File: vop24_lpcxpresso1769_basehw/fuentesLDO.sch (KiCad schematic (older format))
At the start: 21 parts, among them J101 Conn_01x03_Male, U101 MCP1700T-3302E_TT, U102 MCP1700T-3302E_TT, U103 TPS63001

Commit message: PCB: posicionamiento preruteo. ESQ: cambio de footprint de conectores
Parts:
- FB101: symbol dk_Ferrite-Beads-and-Chips:BLM21PG331SN1D -> vop24_lpcxpresso1769_basehw-rescue:BLM21PG331SN1D-dk_Ferrite-Beads-and-Chips
- J101: symbol Connector:Conn_01x03_Male -> vop24_lpcxpresso1769_basehw-rescue:Conn_01x03_Male-Connector
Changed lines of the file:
@@
 DVCC_UD
 $Comp
-L Connector:Conn_01x03_Male J101
+L vop24_lpcxpresso1769_basehw-rescue:Conn_01x03_Male-Connector J101
 U 1 1 5BC24F14
 P 9750 3200
+AR Path="/5BC24F14" Ref="J101"  Part="1"
+AR Path="/5B3826CA/5BC24F14" Ref="J101"  Part="1"
 F 0 "J101" H 9856 3478 50  0000 C CNN
 F 1 "Conn_01x03_Male" H 9856 3387 50  0000 C CNN
@@
 	8900 3200 9550 3200
 $Comp
-L dk_Ferrite-Beads-and-Chips:BLM21PG331SN1D FB101
+L vop24_lpcxpresso1769_basehw-rescue:BLM21PG331SN1D-dk_Ferrite-Beads-and-Chips FB101
 U 1 1 5BD41945
 P 5500 6400
+AR Path="/5BD41945" Ref="FB101"  Part="1"
+AR Path="/5B3826CA/5BD41945" Ref="FB101"  Part="1"
 F 0 "FB101" H 5500 6687 60  0000 C CNN
 F 1 "BLM21PG331SN1D" H 5500 6581 60  0000 C CNN

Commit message: PCB: ruteo de fuentes.    SCH: separacion de pistas de masa en fuentes
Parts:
- added R101: 0, Resistor_SMD:R_0805_2012Metric_Pad1.15x1.40mm_HandSolder, symbol Device:R_Small
- renumbered R101 to R102, R102 to R103, R103 to R104, R104 to R105, R105 to R106
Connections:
- wire segments 95 -> 96
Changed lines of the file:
@@
 $EndComp
 $Comp
-L Device:R_Small R101
+L Device:R_Small R102
 U 1 1 5B383133
 P 3250 4150
-F 0 "R101" V 3150 4050 50  0000 L CNN
+F 0 "R102" V 3150 4050 50  0000 L CNN
 F 1 "0" V 3200 4250 50  0000 L CNN
 F 2 "Resistor_SMD:R_0805_2012Metric_Pad1.15x1.40mm_HandSolder" H 3250 4150 50  0001 C CNN
@@
 $EndComp
 $Comp
-L Device:R_Small R102
+L Device:R_Small R103
 U 1 1 5B38313A
 P 3300 5350
-F 0 "R102" V 3200 5250 50  0000 L CNN
+F 0 "R103" V 3200 5250 50  0000 L CNN
 F 1 "0" V 3250 5500 50  0000 L CNN
 F 2 "Resistor_SMD:R_0805_2012Metric_Pad1.15x1.40mm_HandSolder" H 3300 5350 50  0001 C CNN
@@
 	0    1    1    0
 $EndComp
-Text Label 5000 3500 0    60   ~ 0
-DVCC
 Text Label 5000 4150 0    60   ~ 0
 DGND
@@
 $EndComp
 $Comp
-L Device:R_Small R104
+L Device:R_Small R105
 U 1 1 5B38314E
 P 5950 4000
-F 0 "R104" H 5980 4020 50  0000 L CNN
+F 0 "R105" H 5980 4020 50  0000 L CNN
 F 1 "1k" H 5980 3960 50  0000 L CNN
 F 2 "Resistor_SMD:R_0805_2012Metric_Pad1.15x1.40mm_HandSolder" H 5950 4000 50  0001 C CNN
@@
 $EndComp
 $Comp
-L Device:R_Small R105
+L Device:R_Small R106
 U 1 1 5B38315C
 P 5950 5200
-F 0 "R105" H 5980 5220 50  0000 L CNN
+F 0 "R106" H 5980 5220 50  0000 L CNN
 F 1 "1k" H 5980 5160 50  0000 L CNN
 F 2 "Resistor_SMD:R_0805_2012Metric_Pad1.15x1.40mm_HandSolder" H 5950 5200 50  0001 C CNN
@@
 $EndComp
 $Comp
-L Device:R R103
+L Device:R R104
 U 1 1 5BBFC68E
 P 4600 2300
-F 0 "R103" H 4670 2346 50  0000 L CNN
+F 0 "R104" H 4670 2346 50  0000 L CNN
 F 1 "100" H 4670 2255 50  0000 L CNN
 F 2 "Resistor_SMD:R_0805_2012Metric_Pad1.15x1.40mm_HandSolder" V 4530 2300 50  0001 C CNN
@@
 Wire Wire Line
 	2700 3600 2700 3000
-Wire Wire Line
-	2700 3000 3800 3000
 Connection ~ 2700 3600
 Wire Wire Line
 	2700 3600 2600 3600
-Connection ~ 3800 3000
 Text HLabel 7550 3000 2    60   BiDi ~ 0
 DGND
@@
 DVCC_UD
 $Comp
-L vop24_lpcxpresso1769_basehw-rescue:Conn_01x03_Male-Connector J101
+L vop24_lpcxpresso1769_basehw-rescue:Conn_01x03_Male-Connector J?
 U 1 1 5BC24F14
 P 9750 3200
-AR Path="/5BC24F14" Ref="J101"  Part="1"
+AR Path="/5BC24F14" Ref="J?"  Part="1"
 AR Path="/5B3826CA/5BC24F14" Ref="J101"  Part="1"
 F 0 "J101" H 9856 3478 50  0000 C CNN
@@
 	8900 3200 9550 3200
 $Comp
-L vop24_lpcxpresso1769_basehw-rescue:BLM21PG331SN1D-dk_Ferrite-Beads-and-Chips FB101
+L vop24_lpcxpresso1769_basehw-rescue:BLM21PG331SN1D-dk_Ferrite-Beads-and-Chips FB?
 U 1 1 5BD41945
 P 5500 6400
-AR Path="/5BD41945" Ref="FB101"  Part="1"
+AR Path="/5BD41945" Ref="FB?"  Part="1"
 AR Path="/5B3826CA/5BD41945" Ref="FB101"  Part="1"
 F 0 "FB101" H 5500 6687 60  0000 C CNN
@@
 Wire Wire Line
 	5700 6400 6250 6400
+$Comp
+L Device:R_Small R101
+U 1 1 5BEC88E2
+P 3250 3000
+F 0 "R101" V 3150 2900 50  0000 L CNN
+F 1 "0" V 3200 3100 50  0000 L CNN
+F 2 "Resistor_SMD:R_0805_2012Metric_Pad1.15x1.40mm_HandSolder" H 3250 3000 50  0001 C CNN
+F 3 "" H 3250 3000 50  0001 C CNN
+	1    3250 3000
+	0    1    1    0
+$EndComp
+Wire Wire Line
+	3350 3000 3800 3000
+Connection ~ 3800 3000
+Wire Wire Line
+	3150 3000 2700 3000
 $EndSCHEMATC

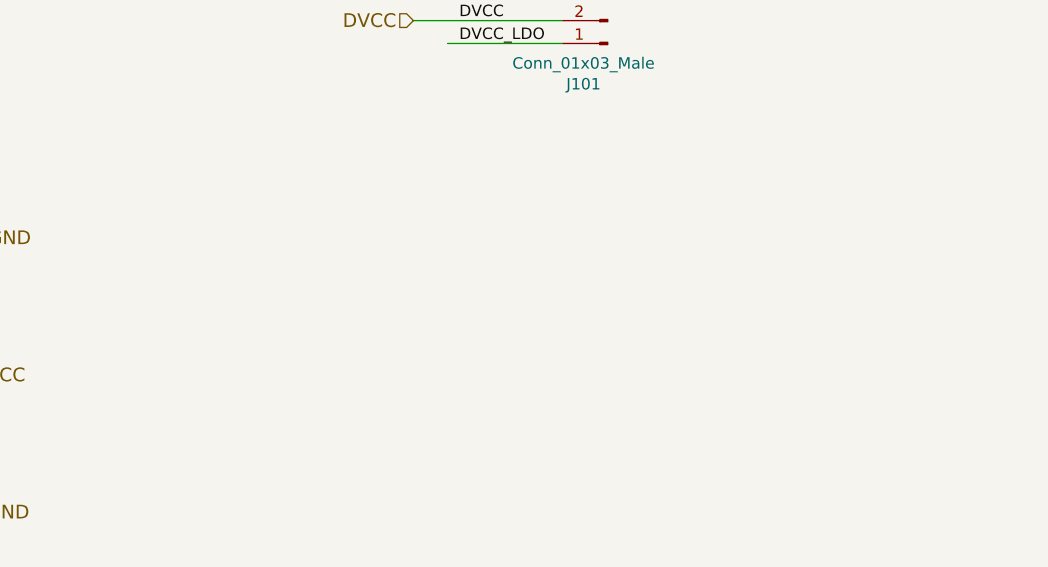
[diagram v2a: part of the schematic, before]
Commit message: Agregado de leyendas en PCB y ESQ. Agregado de cotas en PCB
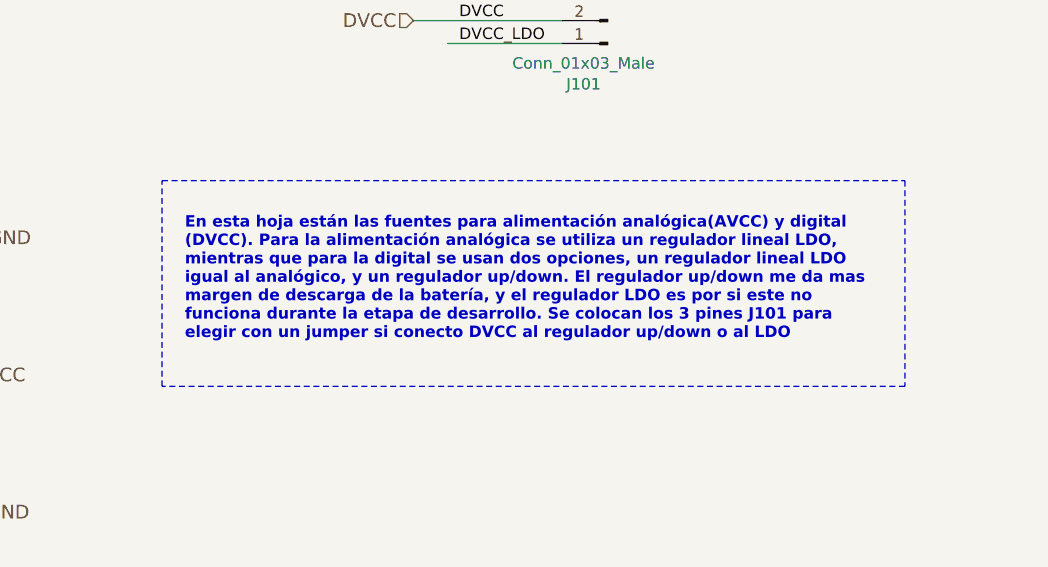
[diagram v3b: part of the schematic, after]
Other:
- note added: "En esta hoja están las fuentes para alimentación analógica(AVCC) y digital\n(DVCC). Para la alimentación analógica se utiliza un regulador lineal LDO,\nmientras que para la digital se usan dos opciones, un regulador lineal LDO\nigual al analógico, y un regulador up/down. El regulador up/down me da mas\nmargen de descarga de la batería, y el regulador LDO es por si este no\nfunciona durante la eta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"
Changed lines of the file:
@@
 encoding utf-8
 Sheet 4 5
-Title ""
-Date ""
-Rev ""
-Comp ""
-Comment1 ""
+Title "VOP24 - Reguladores Analógico y Digital"
+Date "2018-11-01"
+Rev "0.1"
+Comp "Federico G. Roux"
+Comment1 "Universidad Favaloro"
 Comment2 ""
 Comment3 ""
@@
 Wire Wire Line
 	3150 3000 2700 3000
+Text Notes 7900 4600 0    50   ~ 10
+En esta hoja están las fuentes para alimentación analógica(AVCC) y digital\n(DVCC). Para la alimentación analógica se utiliza un regulador lineal LDO,\nmientras que para la digital se usan dos opciones, un regulador lineal LDO\nigual al analógico, y un regulador up/down. El regulador up/down me da mas\nmargen de descarga de la batería, y el regulador LDO es por si este no\nfunciona durante la etapa de desarrollo. Se colocan los 3 pines J101 para\nelegir con un jumper si conecto DVCC al regulador up/down o al LDO\n
+Wire Notes Line
+	7800 3900 11050 3900
+Wire Notes Line
+	11050 3900 11050 4800
+Wire Notes Line
+	11050 4800 7800 4800
+Wire Notes Line
+	7800 4800 7800 3900
 $EndSCHEMATC

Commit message: ESQ: cambios sobre etiquetas y simbolos de POWER
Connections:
- net labels added: GNDA, GNDD, GNDREF, VCOM
- net labels removed: GNDBAT, GND_NREG, VBAT, VCC_NREG
- wire segments 96 -> 99
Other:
- note added: "Tensión no regulada que\nproviene de VUSB si está\nconectado, o de +BATT"
- moved on the sheet: C101, C102, C103, C104, C105, C106, C107, C108, D101, D102, FB101, J101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

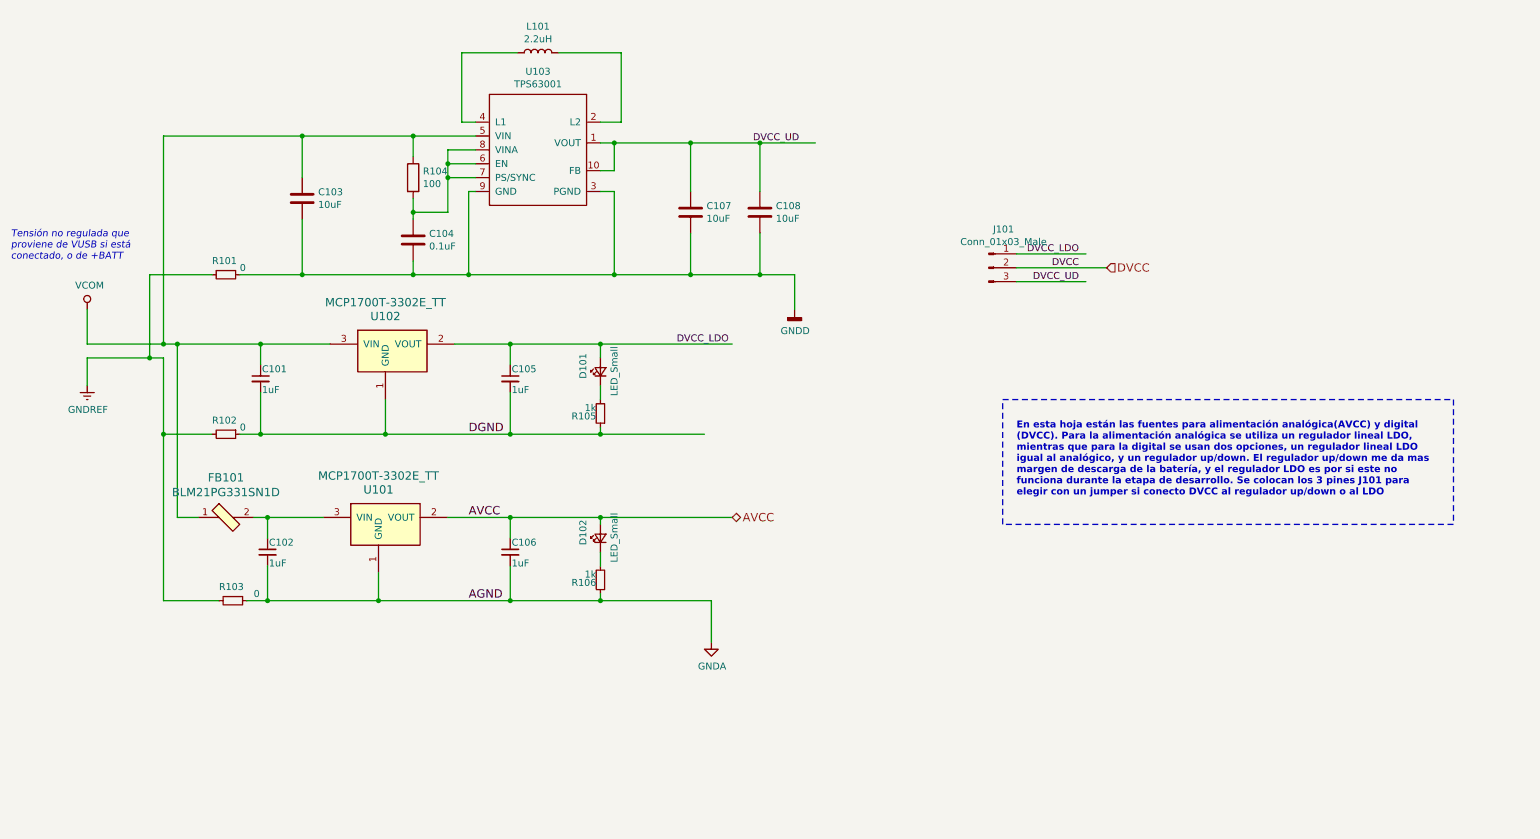
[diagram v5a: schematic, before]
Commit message: ESQ: todas las correcciones atendidas
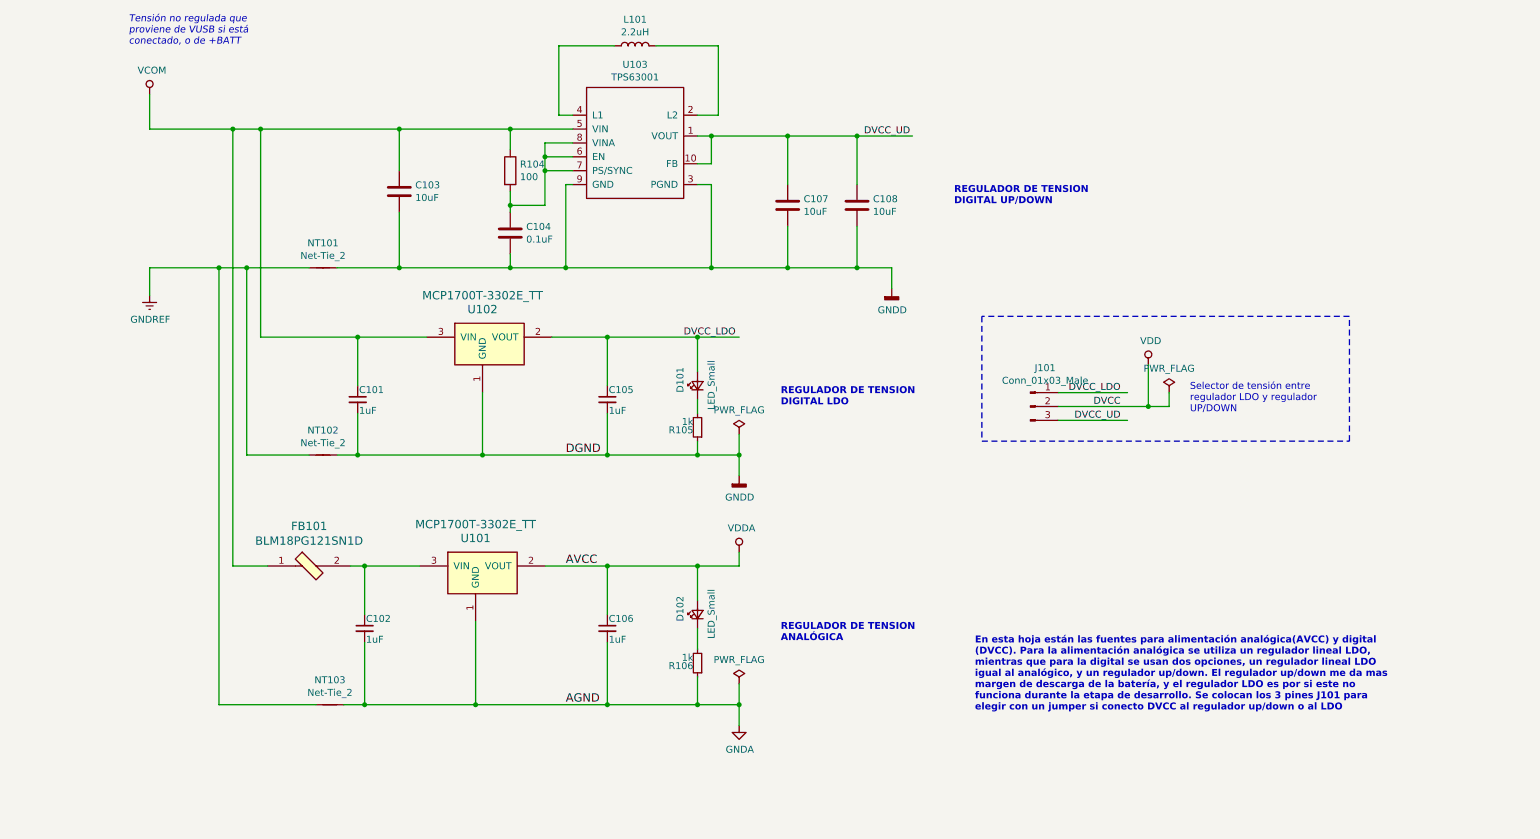
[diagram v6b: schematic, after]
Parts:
- removed FB101: BLM21PG331SN1D, digikey-footprints:0805, symbol vop24_lpcxpresso1769_basehw-rescue:BLM21PG331SN1D-dk_Ferrite-Beads-and-Chips
- removed R101, R102, R103: 0, Resistor_SMD:R_0805_2012Metric_Pad1.15x1.40mm_HandSolder, symbol Device:R_Small
- added FB101: BLM18PG121SN1D, digikey-footprints:0603, symbol vop24_lpcxpresso1769_basehw-rescue:BLM18PG121SN1D
- added NT101, NT102, NT103: Net-Tie_2, symbol Device:Net-Tie_2
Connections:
- net labels added: VDD, VDDA
- wire segments 99 -> 105
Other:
- note added: "REGULADOR DE TENSION\nANALÓGICA"
- note added: "REGULADOR DE TENSION\nDIGITAL LDO"
- note added: "REGULADOR DE TENSION\nDIGITAL UP/DOWN"
- note added: "Selector de tensión entre\nregulador LDO y regulador\nUP/DOWN"
- moved on the sheet: C101, C102, C103, C104, C105, C106, C107, C108, D101, D102, J101, L101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

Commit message: ESQ: cambios en asociaciones de footprints
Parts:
- NT101, NT102, NT103: footprint (none) -> NetTie:NetTie-2_THT_Pad1.0mm
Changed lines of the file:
@@
 F 0 "NT101" H 2900 3128 50  0000 C CNN
 F 1 "Net-Tie_2" H 2900 3037 50  0000 C CNN
-F 2 "" H 2900 2950 50  0001 C CNN
+F 2 "NetTie:NetTie-2_THT_Pad1.0mm" H 2900 2950 50  0001 C CNN
 F 3 "~" H 2900 2950 50  0001 C CNN
 	1    2900 2950
@@
 F 0 "NT102" H 2900 4478 50  0000 C CNN
 F 1 "Net-Tie_2" H 2900 4387 50  0000 C CNN
-F 2 "" H 2900 4300 50  0001 C CNN
+F 2 "NetTie:NetTie-2_THT_Pad1.0mm" H 2900 4300 50  0001 C CNN
 F 3 "~" H 2900 4300 50  0001 C CNN
 	1    2900 4300
@@
 F 0 "NT103" H 2950 6278 50  0000 C CNN
 F 1 "Net-Tie_2" H 2950 6187 50  0000 C CNN
-F 2 "" H 2950 6100 50  0001 C CNN
+F 2 "NetTie:NetTie-2_THT_Pad1.0mm" H 2950 6100 50  0001 C CNN
 F 3 "~" H 2950 6100 50  0001 C CNN
 	1    2950 6100

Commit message: actualizacion de PCB con cambios de ESQ
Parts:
- NT101, NT102, NT103: footprint NetTie:NetTie-2_THT_Pad1.0mm -> NetTie:NetTie-2_SMD_Pad0.5mm
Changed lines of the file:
@@
 F 0 "NT101" H 2900 3128 50  0000 C CNN
 F 1 "Net-Tie_2" H 2900 3037 50  0000 C CNN
-F 2 "NetTie:NetTie-2_THT_Pad1.0mm" H 2900 2950 50  0001 C CNN
+F 2 "NetTie:NetTie-2_SMD_Pad0.5mm" H 2900 2950 50  0001 C CNN
 F 3 "~" H 2900 2950 50  0001 C CNN
 	1    2900 2950
@@
 F 0 "NT102" H 2900 4478 50  0000 C CNN
 F 1 "Net-Tie_2" H 2900 4387 50  0000 C CNN
-F 2 "NetTie:NetTie-2_THT_Pad1.0mm" H 2900 4300 50  0001 C CNN
+F 2 "NetTie:NetTie-2_SMD_Pad0.5mm" H 2900 4300 50  0001 C CNN
 F 3 "~" H 2900 4300 50  0001 C CNN
 	1    2900 4300
@@
 F 0 "NT103" H 2950 6278 50  0000 C CNN
 F 1 "Net-Tie_2" H 2950 6187 50  0000 C CNN
-F 2 "NetTie:NetTie-2_THT_Pad1.0mm" H 2950 6100 50  0001 C CNN
+F 2 "NetTie:NetTie-2_SMD_Pad0.5mm" H 2950 6100 50  0001 C CNN
 F 3 "~" H 2950 6100 50  0001 C CNN
 	1    2950 6100
